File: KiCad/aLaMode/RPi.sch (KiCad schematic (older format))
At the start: 6 parts, among them P1 PBD-26, P2 GPU_JTAG, P3 LAN_JTAG, U6 74LS125

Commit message: aLaMode : work in progress, schematic and PCB. Added Ti level translator
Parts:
- removed B1, B4: I/O, symbol I/O
- removed P1: PBD-26, symbol PBD-26
- removed U6: 74LS125, symbol 74LS125
- added P1: BCM2835_GPIO, symbol BCM2835_GPIO
- added U?: TSX0108, symbol TSX0108
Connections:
- net labels added: 5V0, MISO, MOSI, RST, Rpi_MISO, Rpi_MOSI, Rpi_RST, Rpi_SCLK, SCLK
- wire segments 38 -> 58
- no-connect marks 36 -> 32
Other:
- note removed: "SPARE BUFFER\nwith Break Out Pins"
- moved on the sheet: P2

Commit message: aLaMode work in progress
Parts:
- added C12, C13: 100n, c_0805, symbol C
- gave numbers to parts that had none: 1
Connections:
- net labels added: Rpi_3V3, Rpi_SCK, SCK, U6_OE
- net labels removed: 3V3, Rpi_SCLK, SCLK
- wire segments 58 -> 51
- no-connect marks 32 -> 31
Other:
- note added: "NOTE : How do we handle U6_OE ? Permanently enabled, or via an ATMega Port ?"

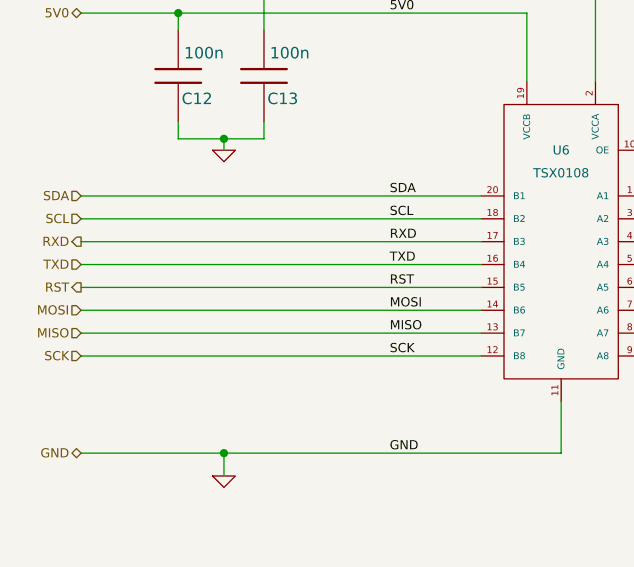
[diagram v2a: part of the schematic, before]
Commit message: aLaMode - preliminary track layout complete
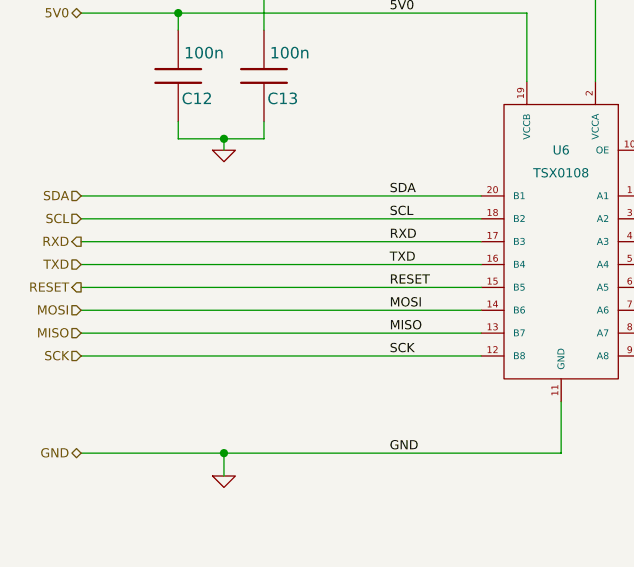
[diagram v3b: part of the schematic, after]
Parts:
- P1, P2, P3: footprint (none) -> pin_strip_7
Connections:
- net labels added: RESET
- net labels removed: RST
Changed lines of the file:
@@
-EESchema Schematic File Version 2  date Monday 11 June 2012 11:32:55 PM IST
+EESchema Schematic File Version 2  date Tuesday 12 June 2012 11:26:21 PM IST
 LIBS:aLaMode
 LIBS:power
@@
 Sheet 4 4
 Title ""
-Date "11 jun 2012"
+Date "12 jun 2012"
 Rev ""
 Comp ""
@@
 MOSI
 Text HLabel 1500 2775 0    40   Output ~ 0
-RST
+RESET
 Text Label 2850 2775 0    40   ~ 0
-RST
+RESET
 Text HLabel 1500 1575 0    40   BiDi ~ 0
 5V0
@@
 F 0 "P1" H 7250 4600 60  0000 C CNN
 F 1 "BCM2835_GPIO" V 7250 3900 50  0000 C CNN
+F 2 "pin_strip_7" H 7250 3900 60  0001 C CNN
 	1    7250 3900
 	1    0    0    -1
@@
 F 0 "P3" H 10650 4600 60  0000 C CNN
 F 1 "LAN_JTAG" V 10770 4200 60  0000 C CNN
+F 2 "pin_strip_7" H 10700 4200 60  0001 C CNN
 	1    10700 4200
 	1    0    0    -1
@@
 F 0 "P2" H 9800 4600 60  0000 C CNN
 F 1 "GPU_JTAG" V 9900 4150 60  0000 C CNN
+F 2 "pin_strip_7" H 9850 4150 60  0001 C CNN
 	1    9850 4150
 	1    0    0    -1

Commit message: aLaMode - some schematic and board changes based on email feedback
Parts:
- removed P3: LAN_JTAG, pin_strip_7, symbol CONN_7
- added P11: U6_OE, pin_strip_2, symbol CONN_3
- added P3: LAN_JTAG, SIL-8, symbol CONN_8
- P1: footprint pin_strip_7 -> pin_array_13x2
- P2: footprint pin_strip_7 -> SIL-8
- U6: footprint (none) -> tssop-20
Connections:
- net labels removed: U6_OE
- wire segments 51 -> 53
- no-connect marks 31 -> 32
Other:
- note removed: "NOTE : How do we handle U6_OE ? Permanently enabled, or via an ATMega Port ?"
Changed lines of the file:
@@
-EESchema Schematic File Version 2  date Tuesday 12 June 2012 11:26:21 PM IST
+EESchema Schematic File Version 2  date Wednesday 13 June 2012 10:25:36 PM IST
 LIBS:aLaMode
 LIBS:power
@@
 Sheet 4 4
 Title ""
-Date "12 jun 2012"
+Date "13 jun 2012"
 Rev ""
 Comp ""
@@
 Comment4 ""
 $EndDescr
+NoConn ~ 10350 3800
+$Comp
+L CONN_8 P3
+U 1 1 4FD8C311
+P 10700 4150
+F 0 "P3" H 10650 4600 60  0000 C CNN
+F 1 "LAN_JTAG" V 10750 4150 60  0000 C CNN
+F 2 "SIL-8" H 10700 4150 60  0001 C CNN
+	1    10700 4150
+	1    0    0    -1
+$EndComp
+Text Label 5850 1875 0    40   ~ 0
+Rpi_3V3
+Wire Wire Line
+	5850 1875 5850 2075
+Wire Wire Line
+	5850 2075 5950 2075
+Wire Wire Line
+	5850 2375 5850 2275
+Wire Wire Line
+	5850 2275 5950 2275
+Wire Wire Line
+	6600 3300 5900 3300
+Connection ~ 2125 2125
+Wire Wire Line
+	2125 2175 2125 2125
+Wire Wire Line
+	2300 1650 2300 1475
+Wire Wire Line
+	1500 1575 3450 1575
+Wire Wire Line
+	3250 2475 1500 2475
+Wire Wire Line
+	3750 1875 3750 1475
+Wire Wire Line
+	3600 3275 3600 3500
+Wire Wire Line
+	3600 3500 1500 3500
+Wire Wire Line
+	3250 2975 1500 2975
+Wire Wire Line
+	3250 2775 1500 2775
+Wire Wire Line
+	3250 2575 1500 2575
+Wire Wire Line
+	6600 4300 4900 4300
+Wire Wire Line
+	4900 4300 4900 2975
+Wire Wire Line
+	4900 2975 3950 2975
+Wire Wire Line
+	3950 2775 8700 2775
+Wire Wire Line
+	8700 2775 8700 3800
+Wire Wire Line
+	3950 2575 8500 2575
+Wire Wire Line
+	8500 2575 8500 3600
+Wire Wire Line
+	8500 3600 7900 3600
+Wire Wire Line
+	6600 3400 5200 3400
+Wire Wire Line
+	5200 3400 5200 2375
+Wire Wire Line
+	5200 2375 3950 2375
+Wire Wire Line
+	8200 3500 7900 3500
+Wire Wire Line
+	6600 3500 5100 3500
+Wire Wire Line
+	5100 3500 5100 2475
+Wire Wire Line
+	5100 2475 3950 2475
+Wire Wire Line
+	7900 3700 8600 3700
+Wire Wire Line
+	8600 3700 8600 2675
+Wire Wire Line
+	8600 2675 3950 2675
+Wire Wire Line
+	6600 4200 5000 4200
+Wire Wire Line
+	5000 4200 5000 2875
+Wire Wire Line
+	5000 2875 3950 2875
+Wire Wire Line
+	6600 4400 4800 4400
+Wire Wire Line
+	4800 4400 4800 3075
+Wire Wire Line
+	4800 3075 3950 3075
+Wire Wire Line
+	1500 2675 3250 2675
+Wire Wire Line
+	1500 2875 3250 2875
+Wire Wire Line
+	1500 3075 3250 3075
+Wire Wire Line
+	3450 1575 3450 1875
+Wire Wire Line
+	3250 2375 1500 2375
+Wire Wire Line
+	8700 3800 7900 3800
+Wire Wire Line
+	3750 1475 2300 1475
+Wire Wire Line
+	1925 1650 1925 1575
+Connection ~ 1925 1575
+Wire Wire Line
+	1925 2050 1925 2125
+Wire Wire Line
+	1925 2125 2300 2125
+Wire Wire Line
+	2300 2125 2300 2050
+Wire Wire Line
+	2125 3600 2125 3500
+Connection ~ 2125 3500
+Wire Wire Line
+	6350 3225 6350 3300
 Connection ~ 6350 3300
 Wire Wire Line
-	6350 3225 6350 3300
-Connection ~ 2125 3500
-Wire Wire Line
-	2125 3600 2125 3500
-Wire Wire Line
-	2300 2050 2300 2125
-Wire Wire Line
-	2300 2125 1925 2125
-Wire Wire Line
-	1925 2125 1925 2050
-Connection ~ 1925 1575
-Wire Wire Line
-	1925 1650 1925 1575
-Wire Wire Line
-	1500 1125 5200 1125
-Wire Wire Line
-	5200 1125 5200 2175
-Wire Wire Line
-	5200 2175 3950 2175
-Wire Wire Line
-	3750 1475 2300 1475
-Wire Wire Line
-	7900 3800 8700 3800
-Wire Wire Line
-	3250 2375 1500 2375
-Wire Wire Line
-	3450 1875 3450 1575
-Wire Wire Line
-	1500 3075 3250 3075
-Wire Wire Line
-	1500 2875 3250 2875
-Wire Wire Line
-	1500 2675 3250 2675
-Wire Wire Line
-	3950 3075 4800 3075
-Wire Wire Line
-	4800 3075 4800 4400
-Wire Wire Line
-	4800 4400 6600 4400
-Wire Wire Line
-	3950 2875 5000 2875
-Wire Wire Line
-	5000 2875 5000 4200
-Wire Wire Line
-	5000 4200 6600 4200
-Wire Wire Line
-	3950 2675 8600 2675
-Wire Wire Line
-	8600 2675 8600 3700
-Wire Wire Line
-	8600 3700 7900 3700
-Wire Wire Line
-	3950 2475 5100 2475
-Wire Wire Line
-	5100 2475 5100 3500
-Wire Wire Line
-	5100 3500 6600 3500
-Wire Wire Line
-	8200 3500 7900 3500
-Wire Wire Line
-	3950 2375 5200 2375
-Wire Wire Line
-	5200 2375 5200 3400
-Wire Wire Line
-	5200 3400 6600 3400
-Wire Wire Line
-	7900 3600 8500 3600
-Wire Wire Line
-	8500 3600 8500 2575
-Wire Wire Line
-	8500 2575 3950 2575
-Wire Wire Line
-	8700 3800 8700 2775
-Wire Wire Line
-	8700 2775 3950 2775
-Wire Wire Line
-	3950 2975 4900 2975
-Wire Wire Line
-	4900 2975 4900 4300
-Wire Wire Line
-	4900 4300 6600 4300
-Wire Wire Line
-	3250 2575 1500 2575
-Wire Wire Line
-	3250 2775 1500 2775
-Wire Wire Line
-	3250 2975 1500 2975
-Wire Wire Line
-	1500 3500 3600 3500
-Wire Wire Line
-	3600 3500 3600 3275
-Wire Wire Line
-	3750 1475 3750 1875
-Wire Wire Line
-	3250 2475 1500 2475
-Wire Wire Line
-	3450 1575 1500 1575
-Wire Wire Line
-	2300 1475 2300 1650
-Wire Wire Line
-	2125 2175 2125 2125
-Connection ~ 2125 2125
-Wire Wire Line
-	6600 3300 5900 3300
-$Comp
-L PWR_FLAG #FLG020
+	5950 2175 3950 2175
+$Comp
+L GND #PWR020
+U 1 1 4FD8C28A
+P 5850 2375
+F 0 "#PWR020" H 5850 2375 30  0001 C CNN
+F 1 "GND" H 5850 2305 30  0001 C CNN
+	1    5850 2375
+	1    0    0    -1
+$EndComp
+$Comp
+L CONN_3 P11
+U 1 1 4FD8C245
+P 6300 2175
+F 0 "P11" V 6250 2175 50  0000 C CNN
+F 1 "U6_OE" V 6350 2175 50  0000 C CNN
+F 2 "pin_strip_2" H 6300 2125 60  0001 C CNN
+	1    6300 2175
+	1    0    0    -1
+$EndComp
+$Comp
+L PWR_FLAG #FLG021
 U 1 1 4FD632B4
 P 6350 3225
-F 0 "#FLG020" H 6350 3495 30  0001 C CNN
+F 0 "#FLG021" H 6350 3495 30  0001 C CNN
 F 1 "PWR_FLAG" H 6350 3455 30  0000 C CNN
 	1    6350 3225
@@
 Rpi_3V3
 $Comp
-L GND #PWR021
+L GND #PWR022
 U 1 1 4FD62C0F
 P 2125 2175
-F 0 "#PWR021" H 2125 2175 30  0001 C CNN
+F 0 "#PWR022" H 2125 2175 30  0001 C CNN
 F 1 "GND" H 2125 2105 30  0001 C CNN
 	1    2125 2175
@@
 $EndComp
 $Comp
-L GND #PWR022
+L GND #PWR023
 U 1 1 4FD62BFD
 P 2125 3600
-F 0 "#PWR022" H 2125 3600 30  0001 C CNN
+F 0 "#PWR023" H 2125 3600 30  0001 C CNN
 F 1 "GND" H 2125 3530 30  0001 C CNN
 	1    2125 3600
@@
 	-1   0    0    1
 $EndComp
-Text HLabel 1500 1125 0    40   Input ~ 0
-U6_OE
-Text Notes 2075 1125 0    40   ~ 0
-NOTE : How do we handle U6_OE ? Permanently enabled, or via an ATMega Port ?
-Text Label 1500 1125 0    40   ~ 0
-U6_OE
 Text Label 4150 3075 0    40   ~ 0
 Rpi_SCK
@@
 F 0 "P1" H 7250 4600 60  0000 C CNN
 F 1 "BCM2835_GPIO" V 7250 3900 50  0000 C CNN
-F 2 "pin_strip_7" H 7250 3900 60  0001 C CNN
+F 2 "pin_array_13x2" H 7250 3900 60  0001 C CNN
 	1    7250 3900
 	1    0    0    -1
@@
 F 0 "U6" H 3600 2975 40  0000 C CNN
 F 1 "TSX0108" H 3600 2875 40  0000 C CNN
+F 2 "tssop-20" H 3600 2575 60  0001 C CNN
 	1    3600 2575
 	-1   0    0    -1
@@
 NoConn ~ 9500 3800
 $Comp
-L CONN_7 P3
-U 1 1 4FBF7498
-P 10700 4200
-F 0 "P3" H 10650 4600 60  0000 C CNN
-F 1 "LAN_JTAG" V 10770 4200 60  0000 C CNN
-F 2 "pin_strip_7" H 10700 4200 60  0001 C CNN
-	1    10700 4200
-	1    0    0    -1
-$EndComp
-$Comp
 L CONN_8 P2
 U 1 1 4FBF744D
@@
 F 0 "P2" H 9800 4600 60  0000 C CNN
 F 1 "GPU_JTAG" V 9900 4150 60  0000 C CNN
-F 2 "pin_strip_7" H 9850 4150 60  0001 C CNN
+F 2 "SIL-8" H 9850 4150 60  0001 C CNN
 	1    9850 4150
 	1    0    0    -1

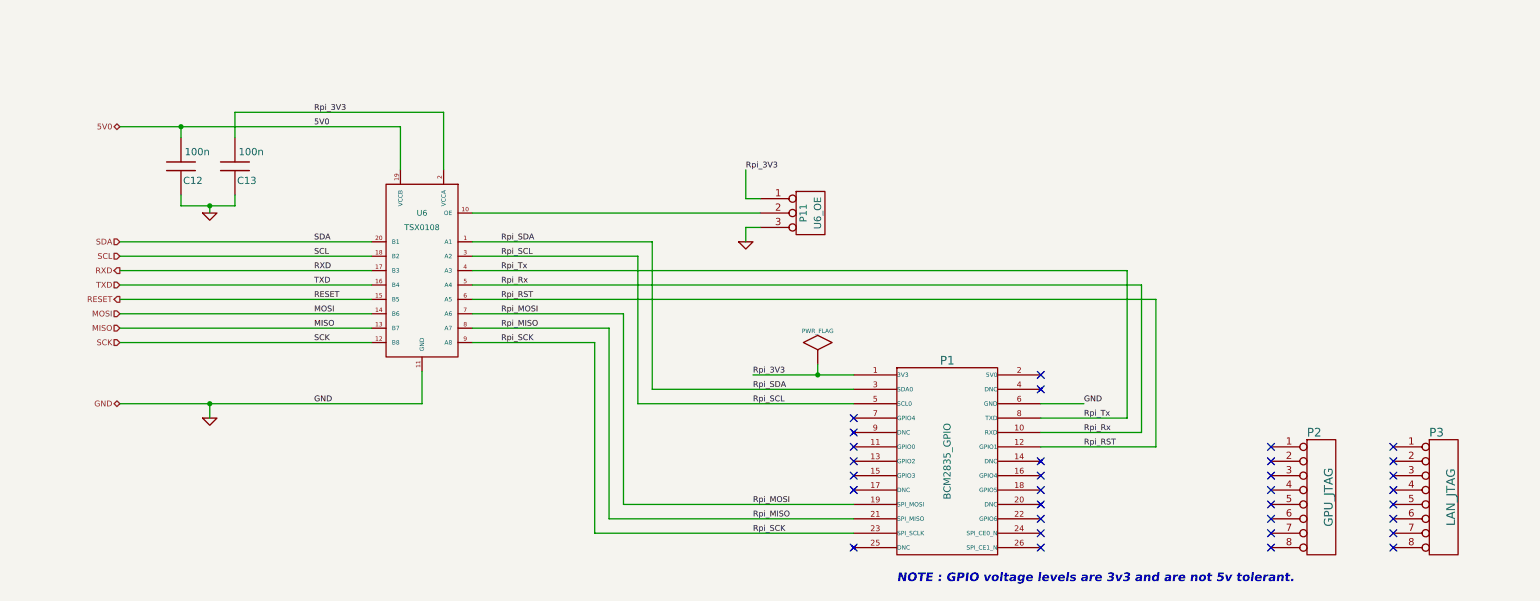
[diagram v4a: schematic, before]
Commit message: aLaMode - track layout complete. Need to add USB Input circuit.
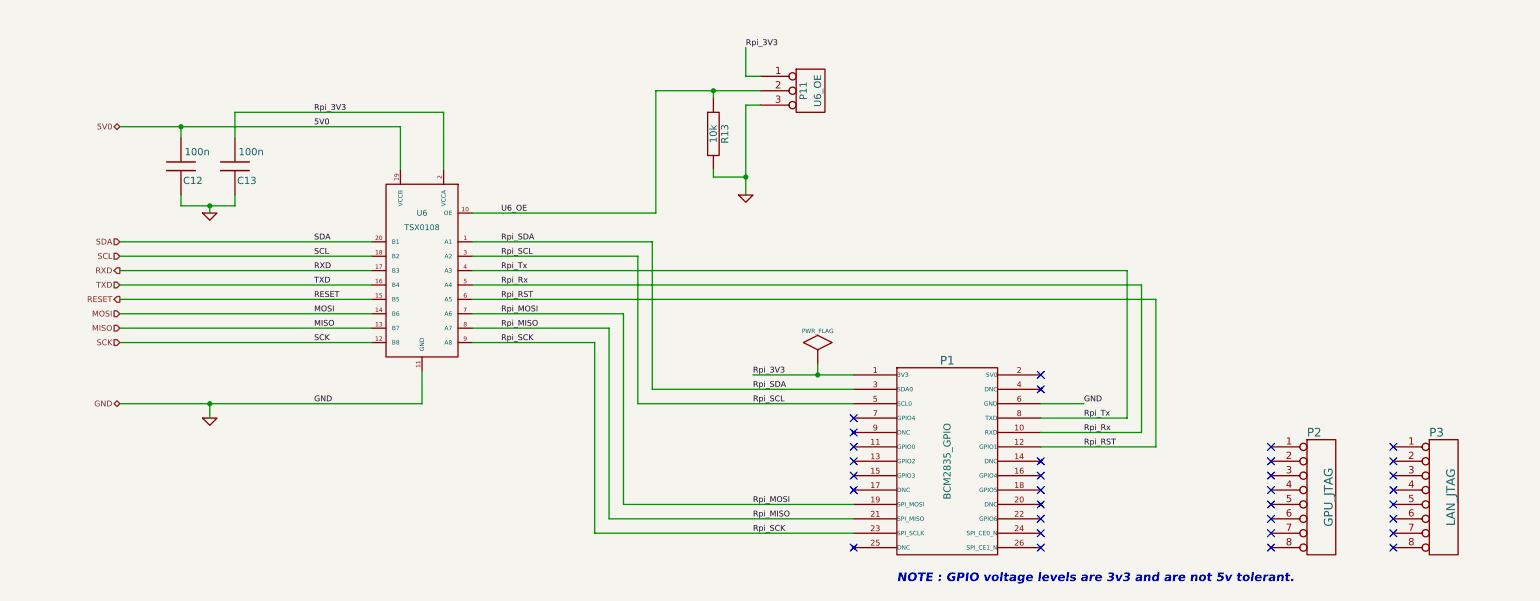
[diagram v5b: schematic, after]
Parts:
- added R13: 10k, r_0805, symbol R
- P1: footprint pin_array_13x2 -> (none)
- P11: footprint pin_strip_2 -> pin_strip_3
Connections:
- net GND: now also R13.2
- net U6_OE: now reaches P11.2 (P2), U6.10 (OE)
- net U6_OE: now also R13.1
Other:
- moved on the sheet: P11
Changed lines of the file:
@@
-EESchema Schematic File Version 2  date Wednesday 13 June 2012 10:25:36 PM IST
+EESchema Schematic File Version 2  date 6/14/2012 6:53:41 PM
 LIBS:aLaMode
 LIBS:power
-LIBS:Conn-raspberry
 LIBS:aLaMode_v1-cache
 EELAYER 25  0
@@
 Sheet 4 4
 Title ""
-Date "13 jun 2012"
+Date "14 jun 2012"
 Rev ""
 Comp ""
@@
 Comment4 ""
 $EndDescr
+$Comp
+L BCM2835_GPIO P1
+U 1 1 4FD9E5BC
+P 7250 3900
+F 0 "P1" H 7250 4600 60  0000 C CNN
+F 1 "BCM2835_GPIO" V 7250 3900 50  0000 C CNN
+	1    7250 3900
+	1    0    0    -1
+$EndComp
+Text Label 4150 2175 0    40   ~ 0
+U6_OE
+Connection ~ 5625 1325
+Wire Wire Line
+	5625 1375 5625 1325
+Connection ~ 5850 1925
+Wire Wire Line
+	5850 1925 5625 1925
+Wire Wire Line
+	5625 1925 5625 1875
+Connection ~ 6350 3300
+Wire Wire Line
+	6350 3225 6350 3300
+Connection ~ 2125 3500
+Wire Wire Line
+	2125 3600 2125 3500
+Wire Wire Line
+	2300 2050 2300 2125
+Wire Wire Line
+	2300 2125 1925 2125
+Wire Wire Line
+	1925 2125 1925 2050
+Connection ~ 1925 1575
+Wire Wire Line
+	1925 1650 1925 1575
+Wire Wire Line
+	3750 1475 2300 1475
+Wire Wire Line
+	7900 3800 8700 3800
+Wire Wire Line
+	3250 2375 1500 2375
+Wire Wire Line
+	3450 1875 3450 1575
+Wire Wire Line
+	1500 3075 3250 3075
+Wire Wire Line
+	1500 2875 3250 2875
+Wire Wire Line
+	1500 2675 3250 2675
+Wire Wire Line
+	3950 3075 4800 3075
+Wire Wire Line
+	4800 3075 4800 4400
+Wire Wire Line
+	4800 4400 6600 4400
+Wire Wire Line
+	3950 2875 5000 2875
+Wire Wire Line
+	5000 2875 5000 4200
+Wire Wire Line
+	5000 4200 6600 4200
+Wire Wire Line
+	3950 2675 8600 2675
+Wire Wire Line
+	8600 2675 8600 3700
+Wire Wire Line
+	8600 3700 7900 3700
+Wire Wire Line
+	3950 2475 5100 2475
+Wire Wire Line
+	5100 2475 5100 3500
+Wire Wire Line
+	5100 3500 6600 3500
+Wire Wire Line
+	8200 3500 7900 3500
+Wire Wire Line
+	3950 2375 5200 2375
+Wire Wire Line
+	5200 2375 5200 3400
+Wire Wire Line
+	5200 3400 6600 3400
+Wire Wire Line
+	7900 3600 8500 3600
+Wire Wire Line
+	8500 3600 8500 2575
+Wire Wire Line
+	8500 2575 3950 2575
+Wire Wire Line
+	8700 3800 8700 2775
+Wire Wire Line
+	8700 2775 3950 2775
+Wire Wire Line
+	3950 2975 4900 2975
+Wire Wire Line
+	4900 2975 4900 4300
+Wire Wire Line
+	4900 4300 6600 4300
+Wire Wire Line
+	3250 2575 1500 2575
+Wire Wire Line
+	3250 2775 1500 2775
+Wire Wire Line
+	3250 2975 1500 2975
+Wire Wire Line
+	1500 3500 3600 3500
+Wire Wire Line
+	3600 3500 3600 3275
+Wire Wire Line
+	3750 1475 3750 1875
+Wire Wire Line
+	3250 2475 1500 2475
+Wire Wire Line
+	3450 1575 1500 1575
+Wire Wire Line
+	2300 1475 2300 1650
+Wire Wire Line
+	2125 2175 2125 2125
+Connection ~ 2125 2125
+Wire Wire Line
+	6600 3300 5900 3300
+Wire Wire Line
+	5950 1425 5850 1425
+Wire Wire Line
+	5850 1425 5850 2050
+Wire Wire Line
+	5950 1225 5850 1225
+Wire Wire Line
+	5850 1225 5850 1025
+Wire Wire Line
+	5950 1325 5225 1325
+Wire Wire Line
+	5225 1325 5225 2175
+Wire Wire Line
+	5225 2175 3950 2175
+$Comp
+L R R13
+U 1 1 4FD98CE2
+P 5625 1625
+F 0 "R13" V 5705 1625 50  0000 C CNN
+F 1 "10k" V 5625 1625 50  0000 C CNN
+F 2 "r_0805" H 5625 1625 60  0001 C CNN
+	1    5625 1625
+	1    0    0    -1
+$EndComp
 NoConn ~ 10350 3800
 $Comp
@@
 	1    0    0    -1
 $EndComp
-Text Label 5850 1875 0    40   ~ 0
+Text Label 5850 1025 0    40   ~ 0
 Rpi_3V3
-Wire Wire Line
-	5850 1875 5850 2075
-Wire Wire Line
-	5850 2075 5950 2075
-Wire Wire Line
-	5850 2375 5850 2275
-Wire Wire Line
-	5850 2275 5950 2275
-Wire Wire Line
-	6600 3300 5900 3300
-Connection ~ 2125 2125
-Wire Wire Line
-	2125 2175 2125 2125
-Wire Wire Line
-	2300 1650 2300 1475
-Wire Wire Line
-	1500 1575 3450 1575
-Wire Wire Line
-	3250 2475 1500 2475
-Wire Wire Line
-	3750 1875 3750 1475
-Wire Wire Line
-	3600 3275 3600 3500
-Wire Wire Line
-	3600 3500 1500 3500
-Wire Wire Line
-	3250 2975 1500 2975
-Wire Wire Line
-	3250 2775 1500 2775
-Wire Wire Line
-	3250 2575 1500 2575
-Wire Wire Line
-	6600 4300 4900 4300
-Wire Wire Line
-	4900 4300 4900 2975
-Wire Wire Line
-	4900 2975 3950 2975
-Wire Wire Line
-	3950 2775 8700 2775
-Wire Wire Line
-	8700 2775 8700 3800
-Wire Wire Line
-	3950 2575 8500 2575
-Wire Wire Line
-	8500 2575 8500 3600
-Wire Wire Line
-	8500 3600 7900 3600
-Wire Wire Line
-	6600 3400 5200 3400
-Wire Wire Line
-	5200 3400 5200 2375
-Wire Wire Line
-	5200 2375 3950 2375
-Wire Wire Line
-	8200 3500 7900 3500
-Wire Wire Line
-	6600 3500 5100 3500
-Wire Wire Line
-	5100 3500 5100 2475
-Wire Wire Line
-	5100 2475 3950 2475
-Wire Wire Line
-	7900 3700 8600 3700
-Wire Wire Line
-	8600 3700 8600 2675
-Wire Wire Line
-	8600 2675 3950 2675
-Wire Wire Line
-	6600 4200 5000 4200
-Wire Wire Line
-	5000 4200 5000 2875
-Wire Wire Line
-	5000 2875 3950 2875
-Wire Wire Line
-	6600 4400 4800 4400
-Wire Wire Line
-	4800 4400 4800 3075
-Wire Wire Line
-	4800 3075 3950 3075
-Wire Wire Line
-	1500 2675 3250 2675
-Wire Wire Line
-	1500 2875 3250 2875
-Wire Wire Line
-	1500 3075 3250 3075
-Wire Wire Line
-	3450 1575 3450 1875
-Wire Wire Line
-	3250 2375 1500 2375
-Wire Wire Line
-	8700 3800 7900 3800
-Wire Wire Line
-	3750 1475 2300 1475
-Wire Wire Line
-	1925 1650 1925 1575
-Connection ~ 1925 1575
-Wire Wire Line
-	1925 2050 1925 2125
-Wire Wire Line
-	1925 2125 2300 2125
-Wire Wire Line
-	2300 2125 2300 2050
-Wire Wire Line
-	2125 3600 2125 3500
-Connection ~ 2125 3500
-Wire Wire Line
-	6350 3225 6350 3300
-Connection ~ 6350 3300
-Wire Wire Line
-	5950 2175 3950 2175
 $Comp
 L GND #PWR020
 U 1 1 4FD8C28A
-P 5850 2375
-F 0 "#PWR020" H 5850 2375 30  0001 C CNN
-F 1 "GND" H 5850 2305 30  0001 C CNN
-	1    5850 2375
+P 5850 2050
+F 0 "#PWR020" H 5850 2050 30  0001 C CNN
+F 1 "GND" H 5850 1980 30  0001 C CNN
+	1    5850 2050
 	1    0    0    -1
 $EndComp
@@
 L CONN_3 P11
 U 1 1 4FD8C245
-P 6300 2175
-F 0 "P11" V 6250 2175 50  0000 C CNN
-F 1 "U6_OE" V 6350 2175 50  0000 C CNN
-F 2 "pin_strip_2" H 6300 2125 60  0001 C CNN
-	1    6300 2175
+P 6300 1325
+F 0 "P11" V 6250 1325 50  0000 C CNN
+F 1 "U6_OE" V 6350 1325 50  0000 C CNN
+F 2 "pin_strip_3" H 6300 1275 60  0001 C CNN
+	1    6300 1325
 	1    0    0    -1
 $EndComp
@@
 Rpi_RST
 $Comp
-L BCM2835_GPIO P1
-U 1 1 4FD5E087
-P 7250 3900
-F 0 "P1" H 7250 4600 60  0000 C CNN
-F 1 "BCM2835_GPIO" V 7250 3900 50  0000 C CNN
-F 2 "pin_array_13x2" H 7250 3900 60  0001 C CNN
-	1    7250 3900
-	1    0    0    -1
-$EndComp
-$Comp
 L TSX0108 U6

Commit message: aLaMode - added micro-USB B Power Input circuit.
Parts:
- P1: footprint (none) -> pin_array_13x2
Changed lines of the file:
@@
-EESchema Schematic File Version 2  date Thursday 14 June 2012 11:00:37 PM IST
+EESchema Schematic File Version 2  date 6/15/2012 5:59:12 PM
 LIBS:aLaMode
 LIBS:power
@@
 Sheet 4 4
 Title ""
-Date "14 jun 2012"
+Date "15 jun 2012"
 Rev ""
 Comp ""
@@
 F 0 "P1" H 7250 4600 60  0000 C CNN
 F 1 "BCM2835_GPIO" V 7250 3900 50  0000 C CNN
+F 2 "pin_array_13x2" V 7350 3900 50  0001 C CNN
 	1    7250 3900
 	1    0    0    -1
